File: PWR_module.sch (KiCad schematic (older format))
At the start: 45 parts, among them J1 CONN_01X01, J2 CONN_01X01, J3 CONN_01X01, Q1 BS250, U1 VTX-214-020-115, U2 RT7297BHZSP, U3 RT7297BHZSP

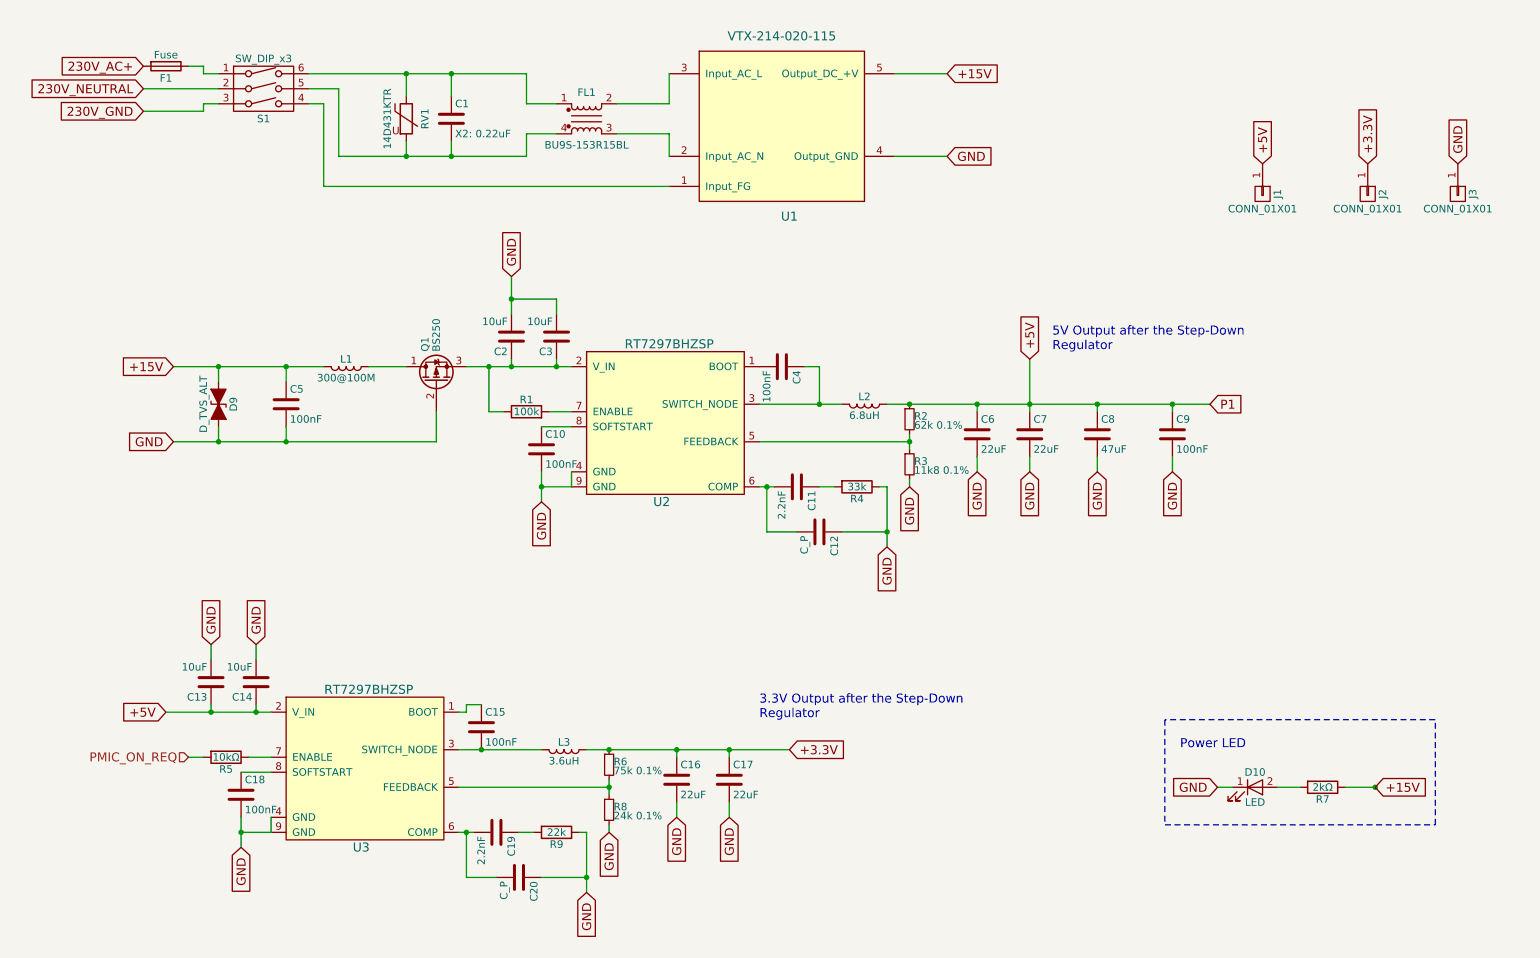
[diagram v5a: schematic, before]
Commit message: I have verified the schematic a second time (except the so-dimm), and I have selected all of the components with links and footprint. I need to verify the schematic a third time and root
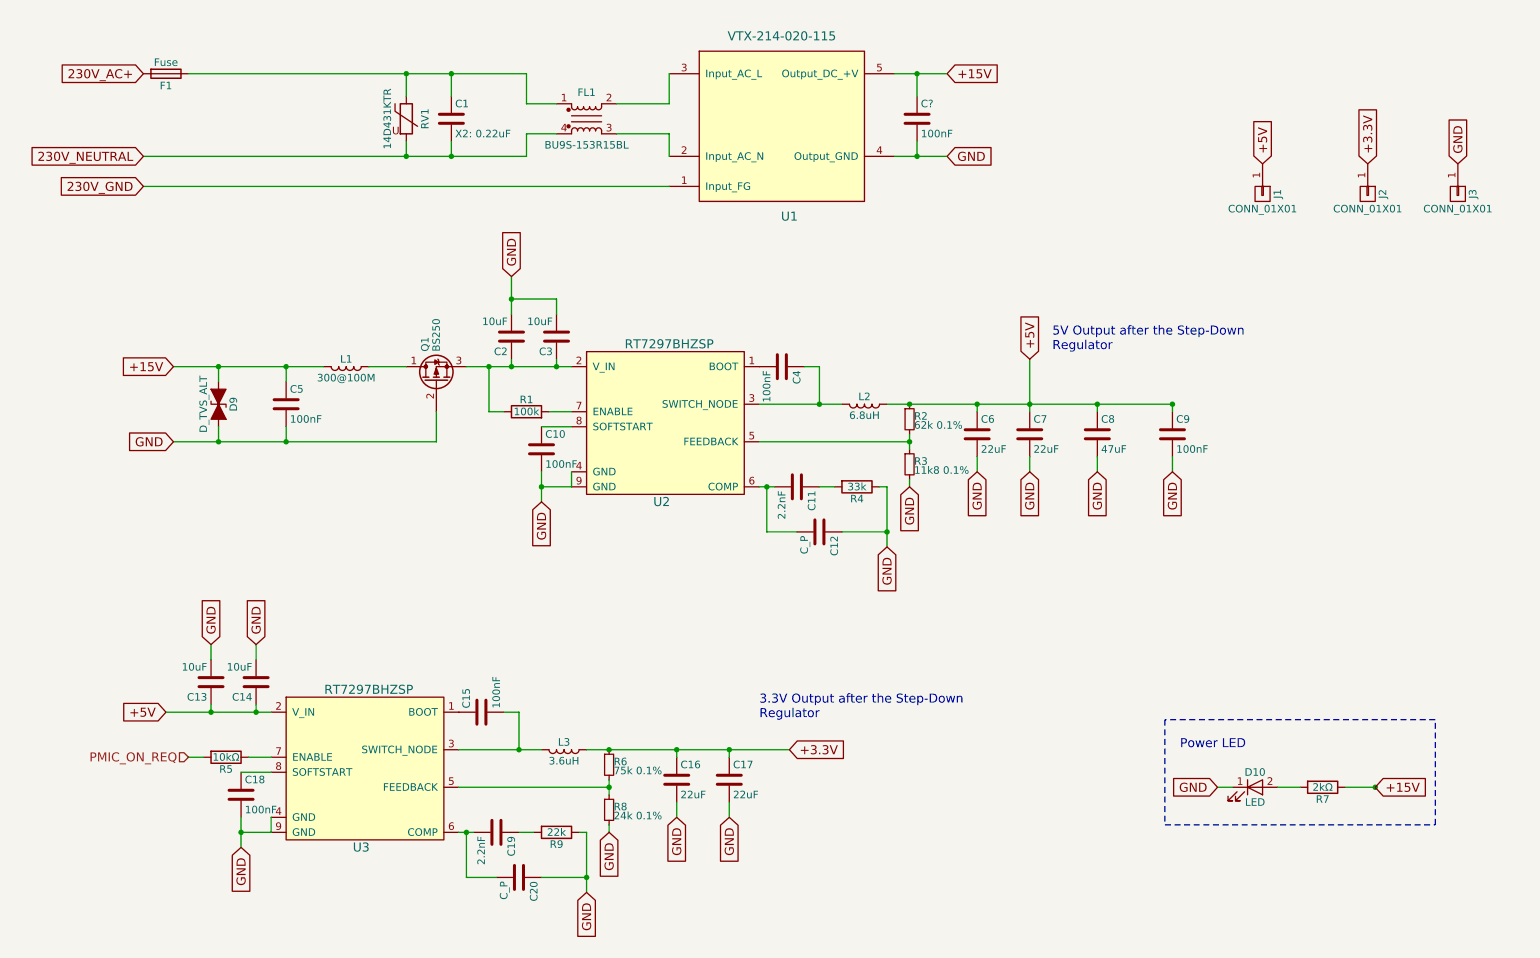
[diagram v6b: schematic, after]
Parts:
- removed S1: SW_DIP_x3, symbol SW_DIP_x3
- added C?: 100nF, Capacitors_SMD:C_0603_HandSoldering, symbol C
- C12: footprint (none) -> Capacitors_SMD:C_0603_HandSoldering
- D9: footprint (none) -> water:P6SMB18CA
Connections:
- net +15V: now also C?.1
- net 230V_GND: now also U1.1 (Input_FG)
- net 230V_NEUTRAL: now also C1.2, FL1.4, RV1.2
- net GND: now also C?.2
- net at F1.1: now also C1.1, FL1.1, RV1.1
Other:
- moved on the sheet: C15, F1
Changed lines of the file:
@@
 Comment4 ""
 $EndDescr
-Text GLabel 1350 1000 0    60   Input ~ 0
+Text GLabel 1350 1050 0    60   Input ~ 0
 230V_AC+
-Text GLabel 1350 1150 0    60   Input ~ 0
+Text GLabel 1350 1600 0    60   Input ~ 0
 230V_NEUTRAL
 $Comp
 L Fuse F1
 U 1 1 592CAA69
-P 1500 1000
-F 0 "F1" V 1580 1000 50  0000 C CNN
-F 1 "Fuse" V 1425 1000 50  0000 C CNN
-F 2 "water:FUSE-0031.8201" V 1430 1000 50  0001 C CNN
-F 3 "http://hu.farnell.com/schurter/0031-8201/fuse-holder-pcb-20x5mm/dp/1162740" H 1500 1000 50  0001 C CNN
-	1    1500 1000
+P 1500 1050
+F 0 "F1" V 1580 1050 50  0000 C CNN
+F 1 "Fuse" V 1425 1050 50  0000 C CNN
+F 2 "water:FUSE-0031.8201" V 1430 1050 50  0001 C CNN
+F 3 "http://hu.farnell.com/schurter/0031-8201/fuse-holder-pcb-20x5mm/dp/1162740" H 1500 1050 50  0001 C CNN
+	1    1500 1050
 	0    1    1    0
 $EndComp
@@
 	1    0    0    -1
 $EndComp
-Text GLabel 1350 1300 0    60   Input ~ 0
+Text GLabel 1350 1800 0    60   Input ~ 0
 230V_GND
 Text GLabel 6700 1600 2    60   Input ~ 0
@@
 Text GLabel 6700 1050 2    60   Input ~ 0
 +15V
-$Comp
-L SW_DIP_x3 S1
-U 1 1 59A4BDAD
-P 2150 1150
-F 0 "S1" H 2150 950 50  0000 C CNN
-F 1 "SW_DIP_x3" H 2150 1350 50  0000 C CNN
-F 2 "" H 2100 1150 60  0000 C CNN
-F 3 "" H 2100 1150 60  0000 C CNN
-	1    2150 1150
-	1    0    0    -1
-$EndComp
 Text GLabel 9550 5800 2    60   Input ~ 0
 +15V
@@
 F 0 "D9" H 1850 3350 50  0000 C CNN
 F 1 "D_TVS_ALT" H 1850 3150 50  0000 C CNN
-F 2 "" H 1850 3250 50  0001 C CNN
-F 3 "" H 1850 3250 50  0001 C CNN
+F 2 "water:P6SMB18CA" H 1850 3250 50  0001 C CNN
+F 3 "http://hu.farnell.com/taiwan-semiconductor/p6smb18ca/tvs-diode-600w-15-3v-bidir-do/dp/2677594" H 1850 3250 50  0001 C CNN
 	1    1850 3250
 	0    1    1    0
@@
 F 0 "C12" H 5875 4200 50  0000 L CNN
 F 1 "C_P" H 5875 4000 50  0000 L CNN
-F 2 "" H 5888 3950 50  0001 C CNN
+F 2 "Capacitors_SMD:C_0603_HandSoldering" H 5888 3950 50  0001 C CNN
 F 3 "" H 5850 4100 50  0001 C CNN
 	1    5850 4100
@@
 	1    0    0    -1
 $EndComp
-Text GLabel 8450 3250 2    60   Input ~ 0
-P1
 Text GLabel 7700 3700 3    60   Input ~ 0
 GND
@@
 	6350 1050 6700 1050
 Wire Wire Line
-	1650 1000 1750 1000
-Wire Wire Line
-	1350 1150 1850 1150
-Wire Wire Line
-	1350 1300 1750 1300
-Wire Wire Line
-	1750 1300 1750 1250
-Wire Wire Line
-	1750 1250 1850 1250
-Wire Wire Line
-	1750 1000 1750 1050
-Wire Wire Line
-	1750 1050 1850 1050
+	1650 1050 3900 1050
 Wire Notes Line
 	8150 5350 8150 6050
@@
 Connection ~ 6300 4100
 Wire Wire Line
-	6300 3250 8450 3250
-Wire Wire Line
 	5450 3500 6450 3500
 Wire Wire Line
@@
 Connection ~ 2100 5300
 Wire Wire Line
-	4000 3900 4000 3700
+	4000 3700 4000 3900
 Wire Wire Line
 	2000 6000 2000 6200
@@
 $EndComp
 Wire Wire Line
-	2650 1600 2650 1150
-Wire Wire Line
-	2650 1150 2450 1150
-Wire Wire Line
-	2450 1250 2550 1250
-Wire Wire Line
-	2550 1250 2550 1800
-Wire Wire Line
-	2550 1800 4850 1800
+	1350 1800 4850 1800
 Wire Wire Line
 	4850 1600 4850 1450
@@
 	3900 1450 3900 1600
 Wire Wire Line
-	3900 1600 2650 1600
+	3900 1600 1350 1600
 Wire Wire Line
 	4850 1050 4850 1250
@@
 Wire Wire Line
 	3900 1250 3900 1050
-Wire Wire Line
-	3900 1050 2450 1050
 Wire Wire Line
 	3100 1200 3100 1050
@@
 L C C15
 U 1 1 59A83D69
-P 3600 5400
-F 0 "C15" H 3625 5500 50  0000 L CNN
-F 1 "100nF" H 3625 5300 50  0000 L CNN
-F 2 "Capacitors_SMD:C_0603_HandSoldering" H 3638 5250 30  0001 C CNN
-F 3 "hu.farnell.com/avx/06035c104kat2a/cap-mlcc-x7r-100nf-50v-0603/dp/1301804" H 3600 5400 60  0001 C CNN
-	1    3600 5400
-	1    0    0    -1
+P 3600 5300
+F 0 "C15" H 3625 5400 50  0000 L CNN
+F 1 "100nF" H 3625 5200 50  0000 L CNN
+F 2 "Capacitors_SMD:C_0603_HandSoldering" H 3638 5150 30  0001 C CNN
+F 3 "hu.farnell.com/avx/06035c104kat2a/cap-mlcc-x7r-100nf-50v-0603/dp/1301804" H 3600 5300 60  0001 C CNN
+	1    3600 5300
+	0    -1   -1   0
 $EndComp
 Wire Wire Line
@@
 Wire Wire Line
 	8200 3600 8200 3700
-Connection ~ 3600 5550
-Wire Wire Line
-	3600 5250 3500 5250
-Wire Wire Line
-	3500 5250 3500 5300
-Wire Wire Line
-	3500 5300 3450 5300
 $Comp
 L C C11
@@
 	0    1    1    0
 $EndComp
+Wire Wire Line
+	3750 5300 3850 5300
+Wire Wire Line
+	3850 5300 3850 5550
+Connection ~ 3850 5550
+Wire Wire Line
+	6300 3250 8200 3250
+$Comp
+L C C?
+U 1 1 59AAEFCC
+P 6500 1350
+F 0 "C?" H 6525 1450 50  0000 L CNN
+F 1 "100nF" H 6525 1250 50  0000 L CNN
+F 2 "Capacitors_SMD:C_0603_HandSoldering" H 6538 1200 30  0001 C CNN
+F 3 "hu.farnell.com/avx/06035c104kat2a/cap-mlcc-x7r-100nf-50v-0603/dp/1301804" H 6500 1350 60  0001 C CNN
+	1    6500 1350
+	1    0    0    -1
+$EndComp
+Wire Wire Line
+	6500 1050 6500 1200
+Connection ~ 6500 1050
+Wire Wire Line
+	6500 1500 6500 1600
+Connection ~ 6500 1600
 $EndSCHEMATC

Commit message: part numbers generated;
pcb generation started
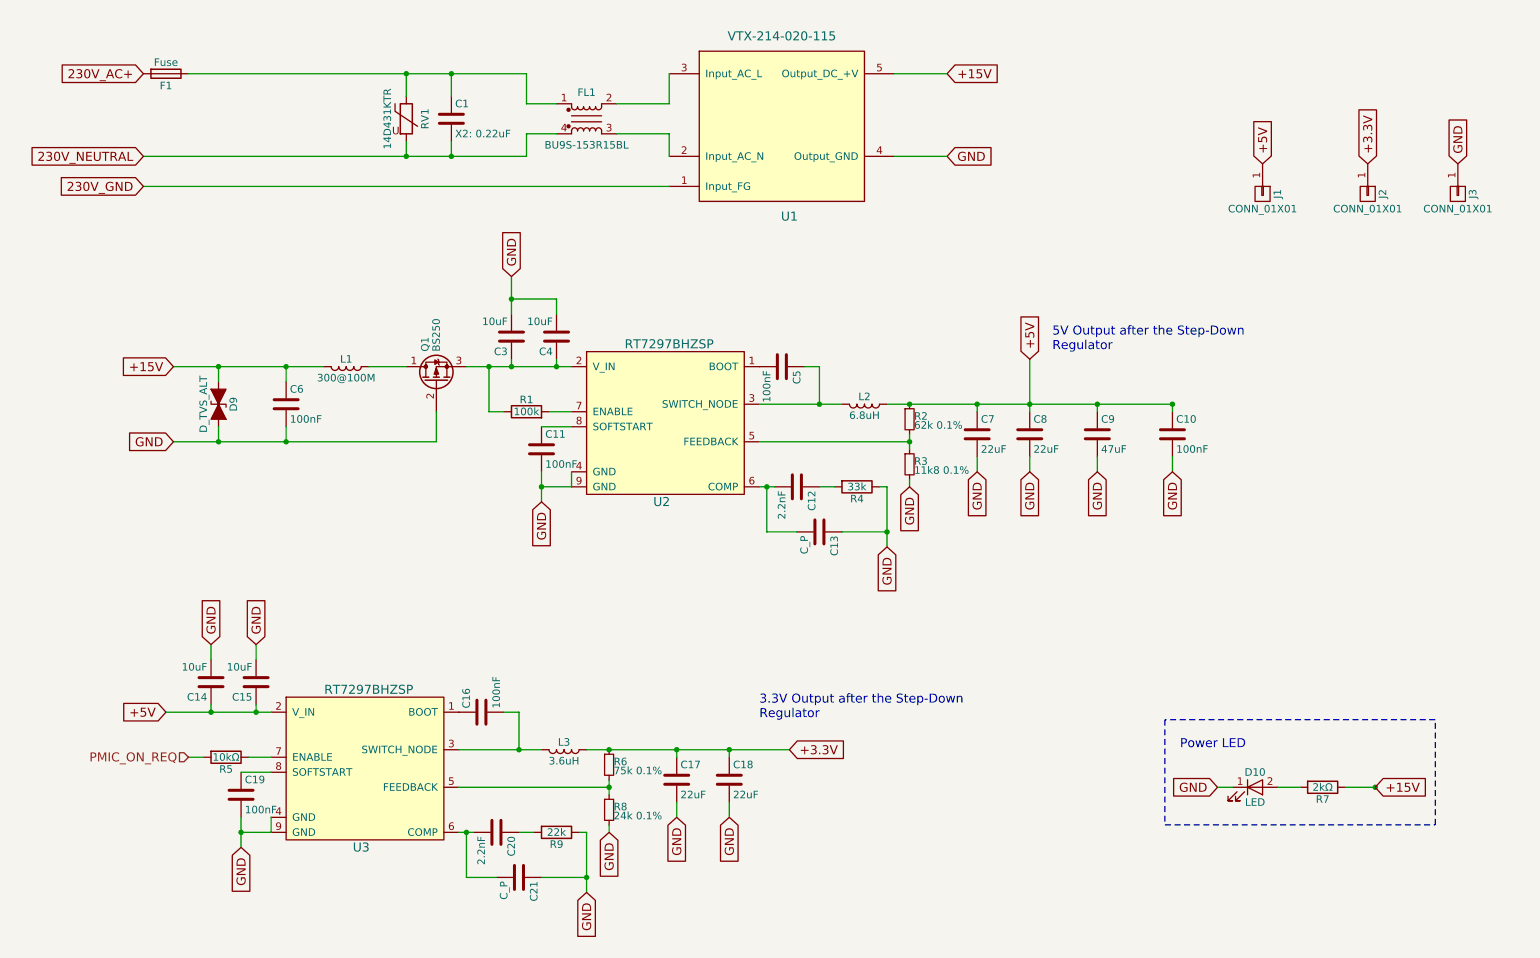
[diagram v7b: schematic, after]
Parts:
- removed C?: 100nF, Capacitors_SMD:C_0603_HandSoldering, symbol C
- C21: renamed from C20; footprint (none) -> Resistors_SMD:R_0603_HandSoldering
- R3: footprint http://hu.farnell.com/te-connectivity/cpf0603b11k8e1/res-thin-film-11k8-0-1-0-063w/dp/2330890 -> Resistors_SMD:R_0603_HandSoldering
- U2, U3: footprint sop:SOP8_ep -> water:SOP8_ep_9GND
- renumbered C9 to C10, C10 to C11, C11 to C12, C12 to C13, C13 to C14, C14 to C15, C15 to C16, C16 to C17, C17 to C18, C18 to C19, C19 to C20, C2 to C3, C3 to C4, C4 to C5, C5 to C6, C6 to C7, C7 to C8, C8 to C9
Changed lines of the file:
@@
 F 0 "U2" H 4800 2700 60  0000 C CNN
 F 1 "RT7297BHZSP" H 4850 3750 60  0000 C CNN
-F 2 "sop:SOP8_ep" H 4600 3300 60  0001 C CNN
+F 2 "water:SOP8_ep_9GND" H 4600 3300 60  0001 C CNN
 F 3 "http://hu.farnell.com/richtek/rt7297bhzsp/dc-dc-conv-sync-buck-1-2mhz-sop/dp/2630201" H 4600 3300 60  0001 C CNN
 	1    4850 3300
@@
 +5V
 $Comp
-L C C12
+L C C13
 U 1 1 59A76882
 P 5850 4100
-F 0 "C12" H 5875 4200 50  0000 L CNN
+F 0 "C13" H 5875 4200 50  0000 L CNN
 F 1 "C_P" H 5875 4000 50  0000 L CNN
 F 2 "Capacitors_SMD:C_0603_HandSoldering" H 5888 3950 50  0001 C CNN
@@
 $EndComp
 $Comp
-L C C8
+L C C9
 U 1 1 59A783A5
 P 7700 3450
-F 0 "C8" H 7725 3550 50  0000 L CNN
+F 0 "C9" H 7725 3550 50  0000 L CNN
 F 1 "47uF" H 7725 3350 50  0000 L CNN
 F 2 "Capacitors_SMD:C_1206_HandSoldering" H 7738 3300 50  0001 C CNN
@@
 F 0 "R3" H 6480 3670 50  0000 L CNN
 F 1 "11k8 0.1%" H 6480 3610 50  0000 L CNN
-F 2 "http://hu.farnell.com/te-connectivity/cpf0603b11k8e1/res-thin-film-11k8-0-1-0-063w/dp/2330890" H 6450 3650 50  0001 C CNN
-F 3 "http://hu.farnell.com/te-connectivity/cpf0603b24ke1/res-thin-film-24k-0-1-0-063w-0603/dp/2331067" H 6450 3650 50  0001 C CNN
+F 2 "Resistors_SMD:R_0603_HandSoldering" H 6450 3650 50  0001 C CNN
+F 3 "http://hu.farnell.com/te-connectivity/cpf0603b11k8e1/res-thin-film-11k8-0-1-0-063w/dp/2330890" H 6450 3650 50  0001 C CNN
 	1    6450 3650
 	1    0    0    -1
@@
 F 0 "U3" H 2800 5000 60  0000 C CNN
 F 1 "RT7297BHZSP" H 2850 6050 60  0000 C CNN
-F 2 "sop:SOP8_ep" H 2600 5600 60  0001 C CNN
+F 2 "water:SOP8_ep_9GND" H 2600 5600 60  0001 C CNN
 F 3 "http://hu.farnell.com/richtek/rt7297bhzsp/dc-dc-conv-sync-buck-1-2mhz-sop/dp/2630201" H 2600 5600 60  0001 C CNN
 	1    2850 5600
@@
 GND
 $Comp
-L C C19
+L C C20
 U 1 1 59A5A4A4
 P 3700 6100
-F 0 "C19" H 3725 6200 50  0000 L CNN
+F 0 "C20" H 3725 6200 50  0000 L CNN
 F 1 "2.2nF" H 3725 6000 50  0000 L CNN
 F 2 "Resistors_SMD:R_0603_HandSoldering" H 3738 5950 50  0001 C CNN
@@
 $EndComp
 $Comp
-L C C16
+L C C17
 U 1 1 59A5A4B8
 P 4900 5750
-F 0 "C16" H 4925 5850 50  0000 L CNN
+F 0 "C17" H 4925 5850 50  0000 L CNN
 F 1 "22uF" H 4925 5650 50  0000 L CNN
 F 2 "Capacitors_SMD:C_0603_HandSoldering" H 4938 5600 50  0001 C CNN
@@
 +3.3V
 $Comp
-L C C20
+L C C21
 U 1 1 59A5A4BF
 P 3850 6400
-F 0 "C20" H 3875 6500 50  0000 L CNN
+F 0 "C21" H 3875 6500 50  0000 L CNN
 F 1 "C_P" H 3875 6300 50  0000 L CNN
-F 2 "" H 3888 6250 50  0001 C CNN
+F 2 "Resistors_SMD:R_0603_HandSoldering" H 3888 6250 50  0001 C CNN
 F 3 "" H 3850 6400 50  0001 C CNN
 	1    3850 6400
@@
 PMIC_ON_REQ
 $Comp
-L C C9
+L C C10
 U 1 1 59A78546
 P 8200 3450
-F 0 "C9" H 8225 3550 50  0000 L CNN
+F 0 "C10" H 8225 3550 50  0000 L CNN
 F 1 "100nF" H 8225 3350 50  0000 L CNN
 F 2 "Capacitors_SMD:C_0603_HandSoldering" H 8238 3300 30  0001 C CNN
@@
 $EndComp
 $Comp
-L C C2
+L C C3
 U 1 1 59A84BFE
 P 3800 2800
-F 0 "C2" H 3825 2900 50  0000 L CNN
+F 0 "C3" H 3825 2900 50  0000 L CNN
 F 1 "10uF" H 3825 2700 50  0000 L CNN
 F 2 "Capacitors_SMD:C_0603_HandSoldering" H 3838 2650 30  0001 C CNN
@@
 $EndComp
 $Comp
-L C C3
+L C C4
 U 1 1 59A84C5F
 P 4100 2800
-F 0 "C3" H 4125 2900 50  0000 L CNN
+F 0 "C4" H 4125 2900 50  0000 L CNN
 F 1 "10uF" H 4125 2700 50  0000 L CNN
 F 2 "Capacitors_SMD:C_0603_HandSoldering" H 4138 2650 30  0001 C CNN
@@
 $EndComp
 $Comp
-L C C13
+L C C14
 U 1 1 59A85396
 P 1800 5100
-F 0 "C13" H 1825 5200 50  0000 L CNN
+F 0 "C14" H 1825 5200 50  0000 L CNN
 F 1 "10uF" H 1825 5000 50  0000 L CNN
 F 2 "Capacitors_SMD:C_0603_HandSoldering" H 1838 4950 30  0001 C CNN
@@
 $EndComp
 $Comp
-L C C14
+L C C15
 U 1 1 59A853FA
 P 2100 5100
-F 0 "C14" H 2125 5200 50  0000 L CNN
+F 0 "C15" H 2125 5200 50  0000 L CNN
 F 1 "10uF" H 2125 5000 50  0000 L CNN
 F 2 "Capacitors_SMD:C_0603_HandSoldering" H 2138 4950 30  0001 C CNN
@@
 Connection ~ 3100 1600
 $Comp
-L C C10
+L C C11
 U 1 1 59A82B13
 P 4000 3550
-F 0 "C10" H 4025 3650 50  0000 L CNN
+F 0 "C11" H 4025 3650 50  0000 L CNN
 F 1 "100nF" H 4025 3450 50  0000 L CNN
 F 2 "Capacitors_SMD:C_0603_HandSoldering" H 4038 3400 30  0001 C CNN
@@
 $EndComp
 $Comp
-L C C4
+L C C5
 U 1 1 59A82CFF
 P 5600 3000
-F 0 "C4" H 5625 3100 50  0000 L CNN
+F 0 "C5" H 5625 3100 50  0000 L CNN
 F 1 "100nF" H 5625 2900 50  0000 L CNN
 F 2 "Capacitors_SMD:C_0603_HandSoldering" H 5638 2850 30  0001 C CNN
@@
 Connection ~ 5850 3250
 $Comp
-L C C18
+L C C19
 U 1 1 59A83AF7
 P 2000 5850
-F 0 "C18" H 2025 5950 50  0000 L CNN
+F 0 "C19" H 2025 5950 50  0000 L CNN
 F 1 "100nF" H 2025 5750 50  0000 L CNN
 F 2 "Capacitors_SMD:C_0603_HandSoldering" H 2038 5700 30  0001 C CNN
@@
 $EndComp
 $Comp
-L C C15
+L C C16
 U 1 1 59A83D69
 P 3600 5300
-F 0 "C15" H 3625 5400 50  0000 L CNN
+F 0 "C16" H 3625 5400 50  0000 L CNN
 F 1 "100nF" H 3625 5200 50  0000 L CNN
 F 2 "Capacitors_SMD:C_0603_HandSoldering" H 3638 5150 30  0001 C CNN
@@
 	6350 1600 6700 1600
 $Comp
-L C C5
+L C C6
 U 1 1 59A87BBB
 P 2300 3250
-F 0 "C5" H 2325 3350 50  0000 L CNN
+F 0 "C6" H 2325 3350 50  0000 L CNN
 F 1 "100nF" H 2325 3150 50  0000 L CNN
 F 2 "Capacitors_SMD:C_0603_HandSoldering" H 2338 3100 30  0001 C CNN
@@
 	8200 3600 8200 3700
 $Comp
-L C C11
+L C C12
 U 1 1 59A8EAB0
 P 5700 3800
-F 0 "C11" H 5725 3900 50  0000 L CNN
+F 0 "C12" H 5725 3900 50  0000 L CNN
 F 1 "2.2nF" H 5725 3700 50  0000 L CNN
 F 2 "Resistors_SMD:R_0603_HandSoldering" H 5738 3650 50  0001 C CNN
@@
 $EndComp
 $Comp
-L C C17
+L C C18
 U 1 1 59A91F73
 P 5250 5750
-F 0 "C17" H 5275 5850 50  0000 L CNN
+F 0 "C18" H 5275 5850 50  0000 L CNN
 F 1 "22uF" H 5275 5650 50  0000 L CNN
 F 2 "Capacitors_SMD:C_0603_HandSoldering" H 5288 5600 50  0001 C CNN
@@
 $EndComp
 $Comp
-L C C6
+L C C7
 U 1 1 59A92510
 P 6900 3450
-F 0 "C6" H 6925 3550 50  0000 L CNN
+F 0 "C7" H 6925 3550 50  0000 L CNN
 F 1 "22uF" H 6925 3350 50  0000 L CNN
 F 2 "Capacitors_SMD:C_0603_HandSoldering" H 6938 3300 50  0001 C CNN
@@
 $EndComp
 $Comp
-L C C7
+L C C8
 U 1 1 59A92696
 P 7250 3450
-F 0 "C7" H 7275 3550 50  0000 L CNN
+F 0 "C8" H 7275 3550 50  0000 L CNN
 F 1 "22uF" H 7275 3350 50  0000 L CNN
 F 2 "Capacitors_SMD:C_0603_HandSoldering" H 7288 3300 50  0001 C CNN
@@
 Wire Wire Line
 	6300 3250 8200 3250
-$Comp
-L C C?
-U 1 1 59AAEFCC
-P 6500 1350
-F 0 "C?" H 6525 1450 50  0000 L CNN
-F 1 "100nF" H 6525 1250 50  0000 L CNN
-F 2 "Capacitors_SMD:C_0603_HandSoldering" H 6538 1200 30  0001 C CNN
-F 3 "hu.farnell.com/avx/06035c104kat2a/cap-mlcc-x7r-100nf-50v-0603/dp/1301804" H 6500 1350 60  0001 C CNN
-	1    6500 1350
-	1    0    0    -1
-$EndComp
-Wire Wire Line
-	6500 1050 6500 1200
-Connection ~ 6500 1050
-Wire Wire Line
-	6500 1500 6500 1600
-Connection ~ 6500 1600
 $EndSCHEMATC
